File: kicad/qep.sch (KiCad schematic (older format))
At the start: 35 parts, among them J1101 tblock, U1101 SI8660BD, U1102 am26ls32a, U1103 am26ls32a, U1104 SI8660BD

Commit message: serigraphi, improve of nets. change of soic 8 footprint
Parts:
- U1101, U1104: footprint Package_SO:SOIC-16W_7.5x10.3mm_P1.27mm -> servo:SOIC-16W_7.5x10.3mm_P1.27mm
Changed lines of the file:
@@
 F 0 "U1104" H 9750 4243 39  0000 C CNN
 F 1 "SI8660BD" H 9750 4168 39  0000 C CNN
-F 2 "Package_SO:SOIC-16W_7.5x10.3mm_P1.27mm" H 9150 4000 60  0001 C CNN
+F 2 "servo:SOIC-16W_7.5x10.3mm_P1.27mm" H 9150 4000 60  0001 C CNN
 F 3 "../doc/datasheets/Si8660.pdf" H 9650 4300 60  0001 C CNN
 	1    9750 3700
@@
 F 0 "U1101" H 1950 4243 39  0000 C CNN
 F 1 "SI8660BD" H 1950 4168 39  0000 C CNN
-F 2 "Package_SO:SOIC-16W_7.5x10.3mm_P1.27mm" H 1350 4000 60  0001 C CNN
+F 2 "servo:SOIC-16W_7.5x10.3mm_P1.27mm" H 1350 4000 60  0001 C CNN
 F 3 "../doc/datasheets/Si8660.pdf" H 1850 4300 60  0001 C CNN
 	1    1950 3700

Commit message: bom bom bom...
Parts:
- C1101, C1102, C1103, C1104, C1105, C1106: value 100nF -> 0.1uF; PartNumber (none) -> CC0603KPX7R7BB104; digikey (none) -> 311-1335-1-ND
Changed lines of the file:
@@
 AR Path="/5E092156/5E3EEFDC" Ref="C1103"  Part="1"
 F 0 "C1103" V 3278 2410 20  0000 L CNN
-F 1 "100nF" V 3321 2410 20  0000 L CNN
+F 1 "0.1uF" V 3321 2410 20  0000 L CNN
 F 2 "servo:C_0603_1608Metric" H 3250 2200 60  0001 C CNN
 F 3 "" H 3250 2300 60  0000 C CNN
+F 4 "CC0603KPX7R7BB104" H 0   0   50  0001 C CNN "PartNumber"
+F 5 "311-1335-1-ND" H 0   0   50  0001 C CNN "digikey"
 	1    3250 2300
 	0    1    1    0
@@
 AR Path="/5E092156/5E413474" Ref="C1102"  Part="1"
 F 0 "C1102" V 2978 2410 20  0000 L CNN
-F 1 "100nF" V 3021 2410 20  0000 L CNN
+F 1 "0.1uF" V 3021 2410 20  0000 L CNN
 F 2 "servo:C_0603_1608Metric" H 2950 2200 60  0001 C CNN
 F 3 "" H 2950 2300 60  0000 C CNN
+F 4 "CC0603KPX7R7BB104" H 0   0   50  0001 C CNN "PartNumber"
+F 5 "311-1335-1-ND" H 0   0   50  0001 C CNN "digikey"
 	1    2950 2300
 	0    1    1    0
@@
 AR Path="/5E092156/5E41F89C" Ref="C1105"  Part="1"
 F 0 "C1105" V 8778 2410 20  0000 L CNN
-F 1 "100nF" V 8821 2410 20  0000 L CNN
+F 1 "0.1uF" V 8821 2410 20  0000 L CNN
 F 2 "servo:C_0603_1608Metric" H 8750 2200 60  0001 C CNN
 F 3 "" H 8750 2300 60  0000 C CNN
+F 4 "CC0603KPX7R7BB104" H 0   0   50  0001 C CNN "PartNumber"
+F 5 "311-1335-1-ND" H 0   0   50  0001 C CNN "digikey"
 	1    8750 2300
 	0    1    1    0
@@
 AR Path="/5E092156/5E41F8B1" Ref="C1104"  Part="1"
 F 0 "C1104" V 8478 2410 20  0000 L CNN
-F 1 "100nF" V 8521 2410 20  0000 L CNN
+F 1 "0.1uF" V 8521 2410 20  0000 L CNN
 F 2 "servo:C_0603_1608Metric" H 8450 2200 60  0001 C CNN
 F 3 "" H 8450 2300 60  0000 C CNN
+F 4 "CC0603KPX7R7BB104" H 0   0   50  0001 C CNN "PartNumber"
+F 5 "311-1335-1-ND" H 0   0   50  0001 C CNN "digikey"
 	1    8450 2300
 	0    1    1    0
@@
 AR Path="/5E092156/5E47665D" Ref="C1106"  Part="1"
 F 0 "C1106" V 10928 3110 20  0000 L CNN
-F 1 "100nF" V 10971 3110 20  0000 L CNN
+F 1 "0.1uF" V 10971 3110 20  0000 L CNN
 F 2 "servo:C_0603_1608Metric" H 10900 2900 60  0001 C CNN
 F 3 "" H 10900 3000 60  0000 C CNN
+F 4 "CC0603KPX7R7BB104" H 0   0   50  0001 C CNN "PartNumber"
+F 5 "311-1335-1-ND" H 0   0   50  0001 C CNN "digikey"
 	1    10900 3000
 	0    1    1    0
@@
 AR Path="/5E092156/5E49C63F" Ref="C1101"  Part="1"
 F 0 "C1101" V 878 3060 20  0000 L CNN
-F 1 "100nF" V 921 3060 20  0000 L CNN
+F 1 "0.1uF" V 921 3060 20  0000 L CNN
 F 2 "servo:C_0603_1608Metric" H 850 2850 60  0001 C CNN
 F 3 "" H 850 2950 60  0000 C CNN
+F 4 "CC0603KPX7R7BB104" H 0   0   50  0001 C CNN "PartNumber"
+F 5 "311-1335-1-ND" H 0   0   50  0001 C CNN "digikey"
 	1    850  2950
 	0    1    1    0

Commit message: more bom...
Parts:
- C1101, C1102, C1103, C1104, C1105, C1106: Description (none) -> CAP CER 0.1UF 16V X7R 0603
- J1101: value tblock -> tblock 2x10 3.81; Description (none) -> 20 Position Terminal Block Header, Male Pins, Shrouded (4 S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; PartNumber (none) -> 1843156; digikey (none) -> 277-6029-ND; price@10 (none) -> 12.49300
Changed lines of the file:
@@
 P 5800 3750
 F 0 "J1101" H 5850 4367 50  0000 C CNN
-F 1 "tblock" H 5850 4276 50  0000 C CNN
+F 1 "tblock 2x10 3.81" H 5850 4276 50  0000 C CNN
 F 2 "servo:tblock02x10_3.81" H 5800 3750 50  0001 C CNN
 F 3 "~" H 5800 3750 50  0001 C CNN
+F 4 "20 Position Terminal Block Header, Male Pins, Shrouded (4 Side) 0.150\" (3.81mm) 90°, Right Angle Through Hole " H 0   0   50  0001 C CNN "Description"
+F 5 "1843156 " H 0   0   50  0001 C CNN "PartNumber"
+F 6 "277-6029-ND" H 0   0   50  0001 C CNN "digikey"
+F 7 "12.49300" H 0   0   50  0001 C CNN "price@10"
 	1    5800 3750
 	1    0    0    -1
@@
 F 4 "CC0603KPX7R7BB104" H 0   0   50  0001 C CNN "PartNumber"
 F 5 "311-1335-1-ND" H 0   0   50  0001 C CNN "digikey"
+F 6 "CAP CER 0.1UF 16V X7R 0603 " H 0   0   50  0001 C CNN "Description"
 	1    3250 2300
 	0    1    1    0
@@
 F 4 "CC0603KPX7R7BB104" H 0   0   50  0001 C CNN "PartNumber"
 F 5 "311-1335-1-ND" H 0   0   50  0001 C CNN "digikey"
+F 6 "CAP CER 0.1UF 16V X7R 0603 " H 0   0   50  0001 C CNN "Description"
 	1    2950 2300
 	0    1    1    0
@@
 F 4 "CC0603KPX7R7BB104" H 0   0   50  0001 C CNN "PartNumber"
 F 5 "311-1335-1-ND" H 0   0   50  0001 C CNN "digikey"
+F 6 "CAP CER 0.1UF 16V X7R 0603 " H 0   0   50  0001 C CNN "Description"
 	1    8750 2300
 	0    1    1    0
@@
 F 4 "CC0603KPX7R7BB104" H 0   0   50  0001 C CNN "PartNumber"
 F 5 "311-1335-1-ND" H 0   0   50  0001 C CNN "digikey"
+F 6 "CAP CER 0.1UF 16V X7R 0603 " H 0   0   50  0001 C CNN "Description"
 	1    8450 2300
 	0    1    1    0
@@
 F 4 "CC0603KPX7R7BB104" H 0   0   50  0001 C CNN "PartNumber"
 F 5 "311-1335-1-ND" H 0   0   50  0001 C CNN "digikey"
+F 6 "CAP CER 0.1UF 16V X7R 0603 " H 0   0   50  0001 C CNN "Description"
 	1    10900 3000
 	0    1    1    0
@@
 F 4 "CC0603KPX7R7BB104" H 0   0   50  0001 C CNN "PartNumber"
 F 5 "311-1335-1-ND" H 0   0   50  0001 C CNN "digikey"
+F 6 "CAP CER 0.1UF 16V X7R 0603 " H 0   0   50  0001 C CNN "Description"
 	1    850  2950
 	0    1    1    0

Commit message: stackup
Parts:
- C1101, C1102, C1103, C1104, C1105, C1106: price@10 (none) -> 0.05800
- U1101, U1104: Description (none) -> General Purpose Digital Isolator 5000Vrms 6 Channel 150Mbps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; PartNumber (none) -> SI8660BD-B-ISR; digikey (none) -> 336-4786-1-ND; price@10 (none) -> 2.75000
- U1102, U1103: Description (none) -> 0/4 Receiver RS422, RS423 16-SOIC; PartNumber (none) -> AM26LS32ACDR; digikey (none) -> 296-1011-1-ND; price@10 (none) -> 0.57800
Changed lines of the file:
@@
 F 2 "servo:SOIC-16W_7.5x10.3mm_P1.27mm" H 9150 4000 60  0001 C CNN
 F 3 "../doc/datasheets/Si8660.pdf" H 9650 4300 60  0001 C CNN
+F 4 "General Purpose Digital Isolator 5000Vrms 6 Channel 150Mbps 35kV/µs CMTI 16-SOIC (0.295\", 7.50mm Width) " H 0   0   50  0001 C CNN "Description"
+F 5 "SI8660BD-B-ISR" H 0   0   50  0001 C CNN "PartNumber"
+F 6 " 336-4786-1-ND" H 0   0   50  0001 C CNN "digikey"
+F 7 "2.75000" H 0   0   50  0001 C CNN "price@10"
 	1    9750 3700
 	1    0    0    -1
@@
 F 2 "servo:SOIC-16W_5.3x10.2mm_P1.27mm" H 9100 3150 50  0001 C CNN
 F 3 "../doc/datasheets/am26ls32a.pdf" H 8100 3700 50  0001 C CNN
+F 4 "0/4 Receiver RS422, RS423 16-SOIC " H 0   0   50  0001 C CNN "Description"
+F 5 "AM26LS32ACDR " H 0   0   50  0001 C CNN "PartNumber"
+F 6 "296-1011-1-ND" H 0   0   50  0001 C CNN "digikey"
+F 7 "0.57800" H 0   0   50  0001 C CNN "price@10"
 	1    8100 4100
 	1    0    0    -1
@@
 F 2 "servo:SOIC-16W_7.5x10.3mm_P1.27mm" H 1350 4000 60  0001 C CNN
 F 3 "../doc/datasheets/Si8660.pdf" H 1850 4300 60  0001 C CNN
+F 4 "General Purpose Digital Isolator 5000Vrms 6 Channel 150Mbps 35kV/µs CMTI 16-SOIC (0.295\", 7.50mm Width) " H 0   0   50  0001 C CNN "Description"
+F 5 "SI8660BD-B-ISR" H 0   0   50  0001 C CNN "PartNumber"
+F 6 " 336-4786-1-ND" H 0   0   50  0001 C CNN "digikey"
+F 7 "2.75000" H 0   0   50  0001 C CNN "price@10"
 	1    1950 3700
 	-1   0    0    -1
@@
 F 2 "servo:SOIC-16W_5.3x10.2mm_P1.27mm" H 4600 3150 50  0001 C CNN
 F 3 "../doc/datasheets/am26ls32a.pdf" H 3600 3700 50  0001 C CNN
+F 4 "0/4 Receiver RS422, RS423 16-SOIC " H 0   0   50  0001 C CNN "Description"
+F 5 "AM26LS32ACDR " H 0   0   50  0001 C CNN "PartNumber"
+F 6 "296-1011-1-ND" H 0   0   50  0001 C CNN "digikey"
+F 7 "0.57800" H 0   0   50  0001 C CNN "price@10"
 	1    3600 4100
 	-1   0    0    -1
@@
 F 5 "311-1335-1-ND" H 0   0   50  0001 C CNN "digikey"
 F 6 "CAP CER 0.1UF 16V X7R 0603 " H 0   0   50  0001 C CNN "Description"
+F 7 "0.05800" H 0   0   50  0001 C CNN "price@10"
 	1    3250 2300
 	0    1    1    0
@@
 F 5 "311-1335-1-ND" H 0   0   50  0001 C CNN "digikey"
 F 6 "CAP CER 0.1UF 16V X7R 0603 " H 0   0   50  0001 C CNN "Description"
+F 7 "0.05800" H 0   0   50  0001 C CNN "price@10"
 	1    2950 2300
 	0    1    1    0
@@
 F 5 "311-1335-1-ND" H 0   0   50  0001 C CNN "digikey"
 F 6 "CAP CER 0.1UF 16V X7R 0603 " H 0   0   50  0001 C CNN "Description"
+F 7 "0.05800" H 0   0   50  0001 C CNN "price@10"
 	1    8750 2300
 	0    1    1    0
@@
 F 5 "311-1335-1-ND" H 0   0   50  0001 C CNN "digikey"
 F 6 "CAP CER 0.1UF 16V X7R 0603 " H 0   0   50  0001 C CNN "Description"
+F 7 "0.05800" H 0   0   50  0001 C CNN "price@10"
 	1    8450 2300
 	0    1    1    0
@@
 F 5 "311-1335-1-ND" H 0   0   50  0001 C CNN "digikey"
 F 6 "CAP CER 0.1UF 16V X7R 0603 " H 0   0   50  0001 C CNN "Description"
+F 7 "0.05800" H 0   0   50  0001 C CNN "price@10"
 	1    10900 3000
 	0    1    1    0
@@
 F 5 "311-1335-1-ND" H 0   0   50  0001 C CNN "digikey"
 F 6 "CAP CER 0.1UF 16V X7R 0603 " H 0   0   50  0001 C CNN "Description"
+F 7 "0.05800" H 0   0   50  0001 C CNN "price@10"
 	1    850  2950
 	0    1    1    0

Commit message: bom copleted
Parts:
- R1101, R1103, R1104, R1106, R1107, R1109, R1110, R1112, R1113, R1115, R1116, R1118, R1119, R1121, R1122, R1124: Description (none) -> 10 kOhms ±5% 0.1W, 1/10W Chip Resistor 0603 (1608 Metric) M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; PartNumber (none) -> RC0603JR-0710KL; digikey (none) -> 311-10KGRCT-ND; price@10 (none) -> 0.01900
- R1102, R1105, R1108, R1111, R1114, R1117, R1120, R1123: Description (none) -> 1 kOhms ±5% 0.1W, 1/10W Chip Resistor 0603 (1608 Metric) Mo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; PartNumber (none) -> RC0603JR-071KL; digikey (none) -> 311-1.0KGRCT-ND; price@10 (none) -> 0.01900

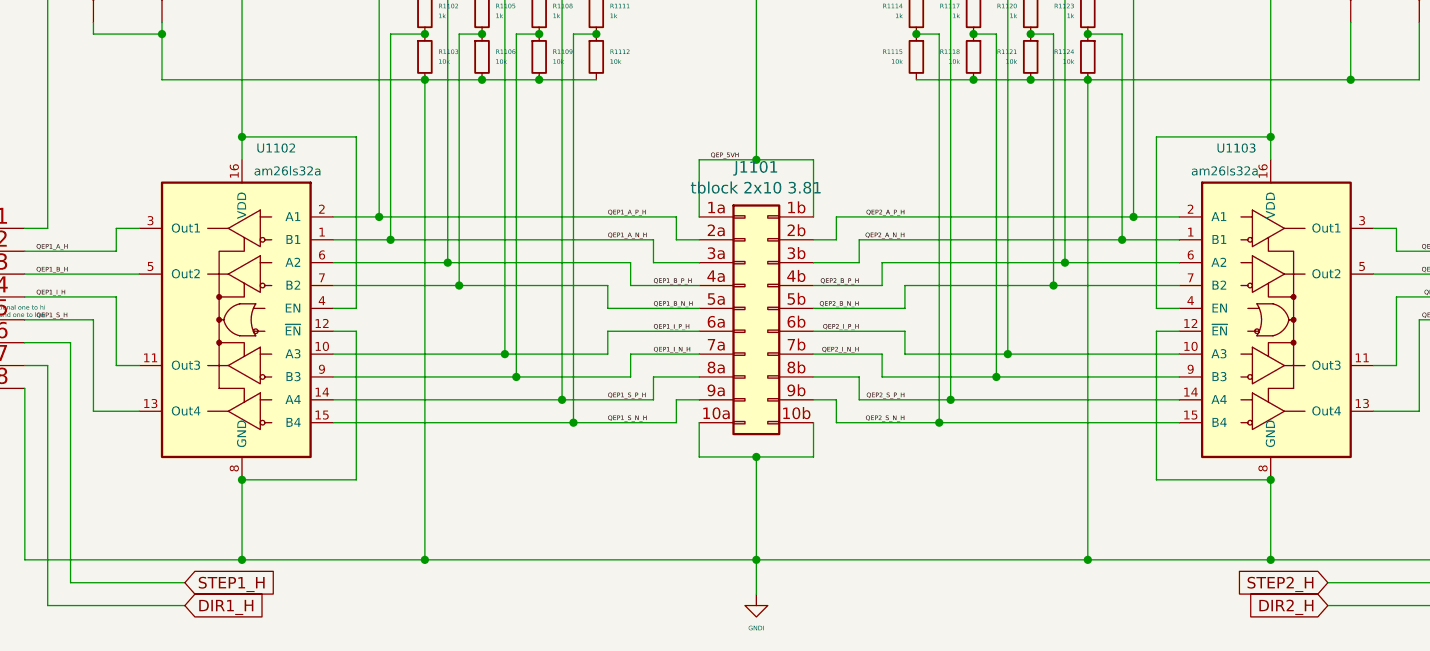
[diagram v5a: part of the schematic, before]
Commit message: changes in footprints
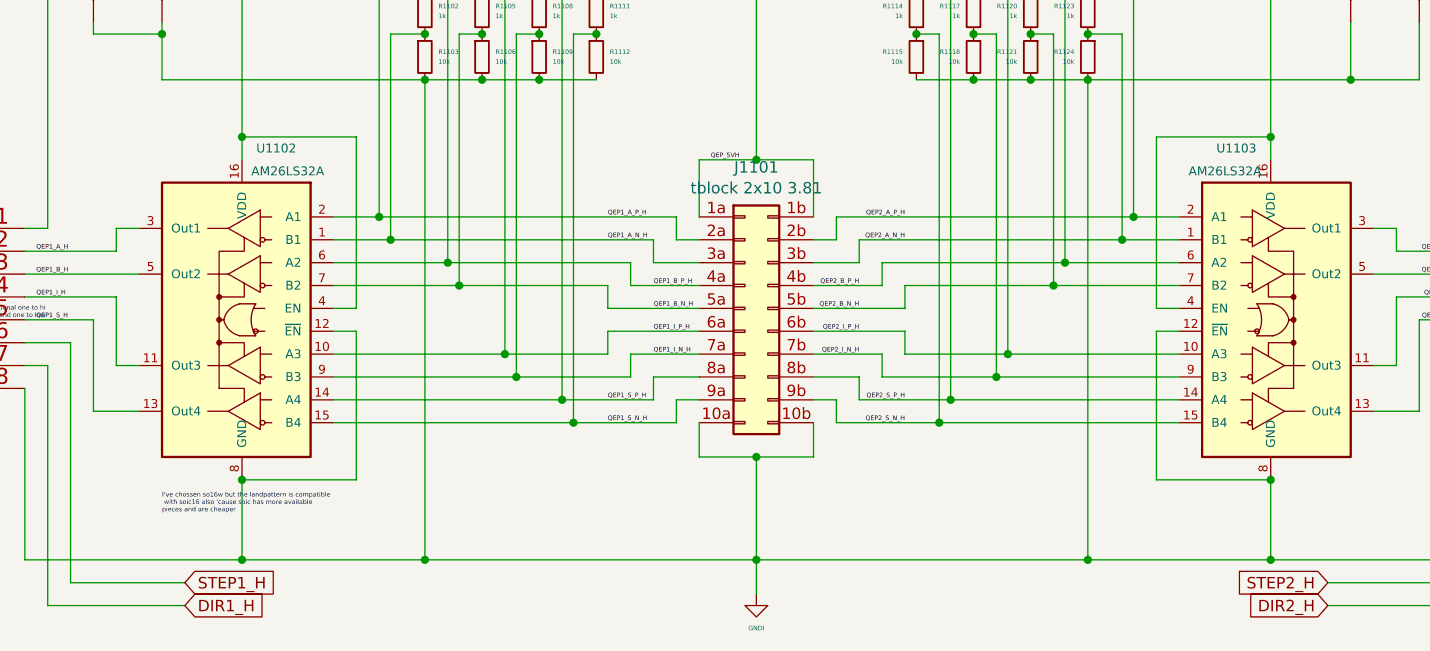
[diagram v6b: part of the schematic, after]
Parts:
- U1102, U1103: value am26ls32a -> AM26LS32A; PartNumber AM26LS32ACDR -> AM26LS32ACDR
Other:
- note added: "I've chossen so16w but the landpattern is compatible\n with soic16 also 'cause soic has more available \npieces and are cheaper"
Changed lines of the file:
@@
 P 8100 4100
 F 0 "U1103" H 7950 5150 39  0000 C CNN
-F 1 "am26ls32a" H 7900 5050 39  0000 C CNN
+F 1 "AM26LS32A" H 7900 5050 39  0000 C CNN
 F 2 "servo:SOIC-16W_5.3x10.2mm_P1.27mm" H 9100 3150 50  0001 C CNN
 F 3 "../doc/datasheets/am26ls32a.pdf" H 8100 3700 50  0001 C CNN
 F 4 "0/4 Receiver RS422, RS423 16-SOIC " H 0   0   50  0001 C CNN "Description"
-F 5 "AM26LS32ACDR " H 0   0   50  0001 C CNN "PartNumber"
+F 5 "AM26LS32ACDR" H 0   0   50  0001 C CNN "PartNumber"
 F 6 "296-1011-1-ND" H 0   0   50  0001 C CNN "digikey"
 F 7 "0.57800" H 0   0   50  0001 C CNN "price@10"
@@
 P 3600 4100
 F 0 "U1102" H 3450 5150 39  0000 C CNN
-F 1 "am26ls32a" H 3400 5050 39  0000 C CNN
+F 1 "AM26LS32A" H 3400 5050 39  0000 C CNN
 F 2 "servo:SOIC-16W_5.3x10.2mm_P1.27mm" H 4600 3150 50  0001 C CNN
 F 3 "../doc/datasheets/am26ls32a.pdf" H 3600 3700 50  0001 C CNN
 F 4 "0/4 Receiver RS422, RS423 16-SOIC " H 0   0   50  0001 C CNN "Description"
-F 5 "AM26LS32ACDR " H 0   0   50  0001 C CNN "PartNumber"
+F 5 "AM26LS32ACDR" H 0   0   50  0001 C CNN "PartNumber"
 F 6 "296-1011-1-ND" H 0   0   50  0001 C CNN "digikey"
 F 7 "0.57800" H 0   0   50  0001 C CNN "price@10"
@@
 Wire Wire Line
 	5850 2050 6550 2050
+Text Notes 3250 4650 0    20   ~ 0
+I've chossen so16w but the landpattern is compatible\n with soic16 also 'cause soic has more available \npieces and are cheaper
 $EndSCHEMATC
